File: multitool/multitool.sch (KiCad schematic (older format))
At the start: 90 parts, among them J1 USB, J14 WS2813, J15 ESP-01, J16 VDDS, J17 MNT, J18 MNT, J19 MNT, J2 SELF_PGM, J20 MNT, J3 UNIVERSAL, J4 WSOUT, J5 VPPS, J6 SAO, J7 VDDS, J8 PADAUK, J9 AVR, Q1 3402, Q2 3402, Q3 3402, Q4 3402, Q5 PNP, SW1 BOOT0, SW2 SUBCFG, U1 STM32F042, U10 3v6, U2 MT2492, U3 NUP4202, U4 3v6, U5 SP485, U6 INA181A3, U7 74LVC02APW, U8 LOADSW, U9 LOADSW

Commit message: update multitool.
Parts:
- removed U1: STM32F042, Package_QFP:TQFP-32_7x7mm_P0.8mm, symbol MCU_ST_STM32F0:STM32F042K4Tx
- added U?: STM32F042C6Tx, Package_QFP:LQFP-48_7x7mm_P0.5mm, symbol MCU_ST_STM32F0:STM32F042C6Tx
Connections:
- net +3V3: now also U?.24 (VDD), U?.36 (VDDIO2), U?.48 (VDD)
- net AVCC: now also U?.9 (VDDA)
- net D+: now also U?.33 (PA12)
- net D-: now also U?.32 (PA11)
- net GND: now also U?.23 (VSS), U?.35 (VSS), U?.47 (VSS), U?.8 (VSSA)
- net NRST: now also U?.7 (NRST)
- net PA10: now also U?.31 (PA10)
- net PIMON: now also U?.17 (PA7)
- net SPIMOSICOMB: now also U?.40 (PB4), U?.41 (PB5)
- net SPISCK: now also U?.39 (PB3)
- net SW1VDD: now also U?.18 (PB0)
- net SW1VPP: now also U?.22 (PB11)
- net SW2VDD: now also U?.19 (PB1)
- net SW2VPP: now also U?.21 (PB10)
- net SWC: now also U?.37 (PA14)
- net SWD: now also U?.34 (PA13)
- net U2CK: no longer R26.1, R27.2
- net U2RTS: now also U?.11 (PA1)
- net U2RX: now also U?.38 (PA15)
- net VMON1: now also U?.10 (PA0)
- net VMON2: now also U?.13 (PA3)
- net ~485RXEN~: now also U?.2 (PC13)
- net BOOT0: now reaches R3.2, SW1.4
- net BOOT0: now also U?.44 (PF11)
- net at R9.2: now also U?.29 (PA8)
- net at R10.2: now also U?.16 (PA6)
- net at R4.2: now also U?.5 (PF0)
- net at R6.2: now also U?.6 (PF1)
- net SUBCFG: now reaches SW2.4
- net SUBCFG: now also U?.3 (PC14)
- net at R12.2: now also U?.42 (PB6), U?.43 (PB7)
- net U2TX renamed U2TXRX
- new net CANRX: U?.45 (PB8)
- new net CANTX: U?.46 (PB9)
- new net VMONIN: R26.1, R27.2, U?.12 (PA2)
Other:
- note added: "T16C1"
- note added: "T2C3\nT2C4"
- note added: "TODO: REDO GPIO"
- note removed: "T1C1\nT1C2"
- note removed: "T2CH3"
- note removed: "U2TX alt is TIM2_CH3"
- moved on the sheet: C10, C19, C23, C25, C6, C7, C8, D23, J2, J5, J7, L3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

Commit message: another shot at multitool
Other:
- note added: "U2RX is 5V tolerant\nSPISCK is 5V tolerant"
- note removed: "U2TX can also function as SPI_NSS\nU2RX is 5V tolerant\nSPISCK is 5V tolerant"
- moved on the sheet: C10, C19, C6, J2, R12, U10, U4

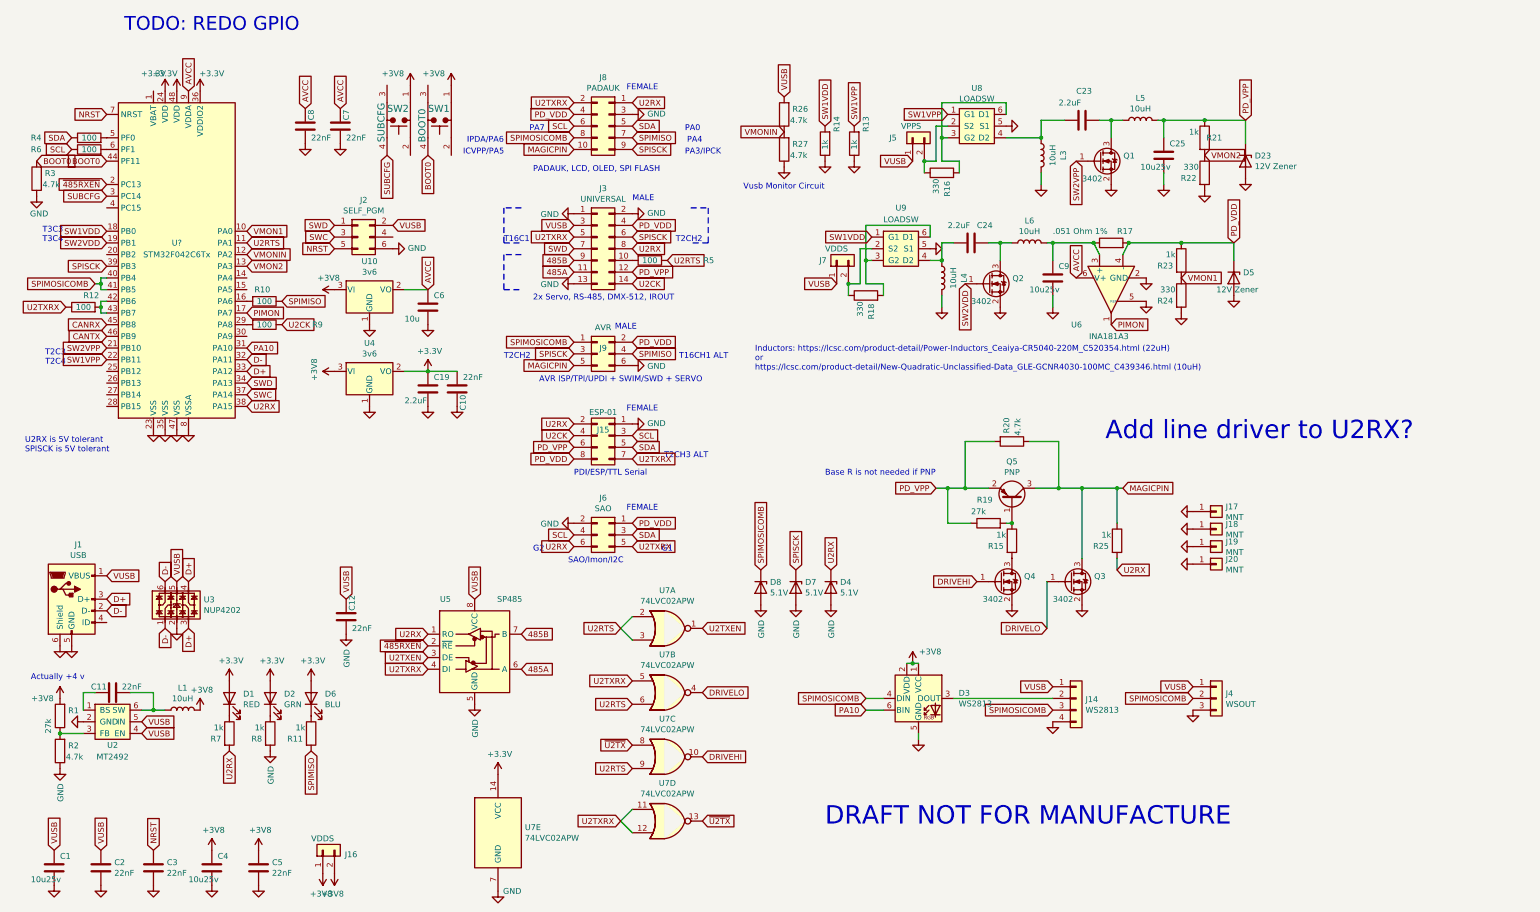
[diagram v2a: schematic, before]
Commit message: Move attempt at can away.
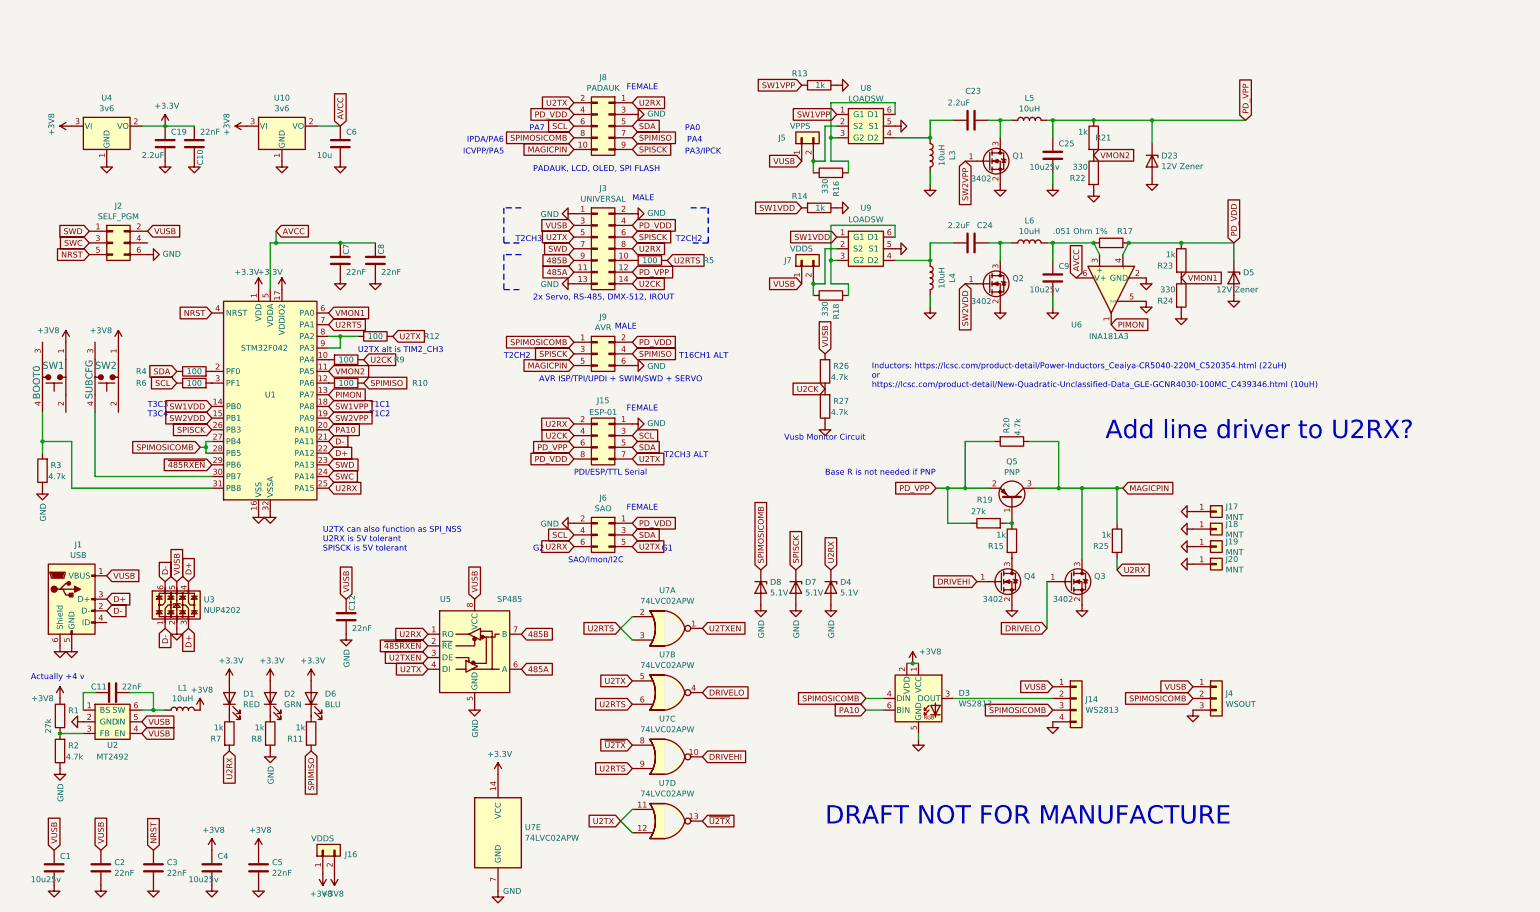
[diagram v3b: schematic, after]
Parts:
- removed U?: STM32F042C6Tx, Package_QFP:LQFP-48_7x7mm_P0.5mm, symbol MCU_ST_STM32F0:STM32F042C6Tx
- added U1: STM32F042, Package_QFP:TQFP-32_7x7mm_P0.8mm, symbol MCU_ST_STM32F0:STM32F042K4Tx
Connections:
- net VMONIN is gone; now on net U2CK: R26.1, R27.2
- net +3V3: now also U1.1 (VDD), U1.17 (VDDIO2)
- net AVCC: now also U1.5 (VDDA)
- net D+: now also U1.22 (PA12)
- net D-: now also U1.21 (PA11)
- net GND: now also U1.16 (VSS), U1.32 (VSSA)
- net NRST: now also U1.4 (NRST)
- net PA10: now also U1.20 (PA10)
- net PIMON: now also U1.13 (PA7)
- net SPIMOSICOMB: now also U1.27 (PB4), U1.28 (PB5)
- net SPISCK: now also U1.26 (PB3)
- net SW1VDD: now also U1.14 (PB0)
- net SW1VPP: now also U1.18 (PA8)
- net SW2VDD: now also U1.15 (PB1)
- net SW2VPP: now also U1.19 (PA9)
- net SWC: now also U1.24 (PA14)
- net SWD: now also U1.23 (PA13)
- net U2RTS: now also U1.7 (PA1)
- net U2RX: now also U1.25 (PA15)
- net VMON1: now also U1.6 (PA0)
- net VMON2: now also U1.11 (PA5)
- net ~485RXEN~: now also U1.29 (PB6)
- net at R4.2: now also U1.2 (PF0)
- net at R6.2: now also U1.3 (PF1)
- net at R9.2: now also U1.10 (PA4)
- net at R12.2: now also U1.8 (PA2), U1.9 (PA3)
- net at R10.2: now also U1.12 (PA6)
- net BOOT0: no longer names the net of R3.2, SW1.4
- net BOOT0: now also U1.31 (PB8)
- net SUBCFG: no longer names the net of SW2.4
- net SUBCFG: now also U1.30 (PB7)
- net U2TXRX renamed U2TX
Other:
- note added: "T1C1\nT1C2"
- note added: "T2CH3"
- note added: "U2TX alt is TIM2_CH3"
- note added: "U2TX can also function as SPI_NSS\nU2RX is 5V tolerant\nSPISCK is 5V tolerant"
- note removed: "T16C1"
- note removed: "T2C3\nT2C4"
- note removed: "TODO: REDO GPIO"
- note removed: "U2RX is 5V tolerant\nSPISCK is 5V tolerant"
- moved on the sheet: C10, C19, C23, C25, C6, C7, C8, D23, J2, J5, J7, L3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
